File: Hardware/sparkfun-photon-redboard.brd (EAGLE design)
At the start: 68.6 x 53.3 mm, 54 parts, among them J1 AMP FCI 10103594-0001LF, U1 WM-N-BM-14

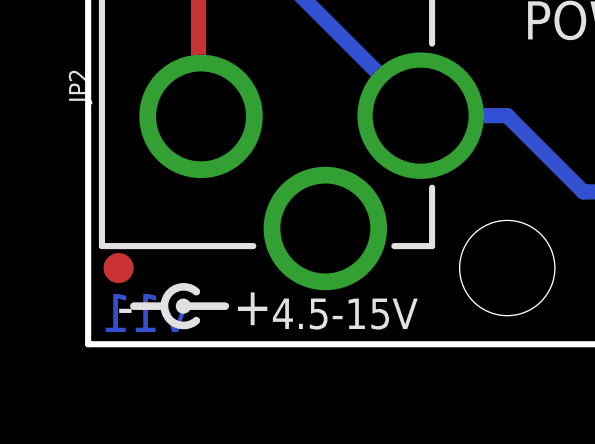
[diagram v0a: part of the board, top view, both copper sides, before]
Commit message: Updated Revision to 2.0 for Reds
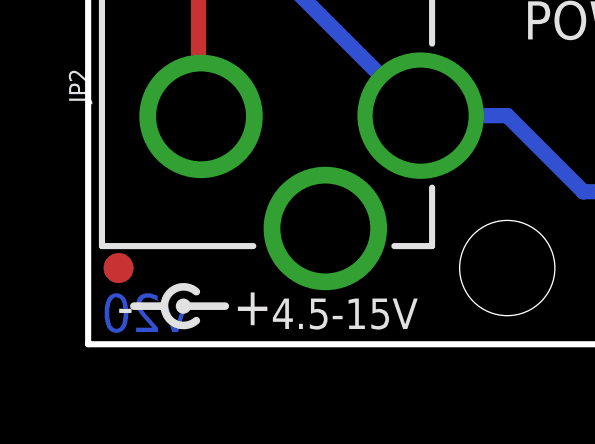
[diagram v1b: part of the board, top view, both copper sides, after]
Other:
- board text added: "v20"
- board text removed: "v11"
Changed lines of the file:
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@@
 <text x="20.32" y="4.064" size="1.27" layer="21" font="vector" ratio="15" rot="R90" align="center-left">VBAT</text>
 <text x="22.86" y="4.064" size="1.27" layer="21" font="vector" ratio="15" rot="R90" align="center-left">GND</text>
-<text x="1.905" y="1.6764" size="1.27" layer="16" font="vector" ratio="15" rot="MR0" align="top-center">v11</text>
+<text x="1.905" y="1.6764" size="1.27" layer="16" font="vector" ratio="15" rot="MR0" align="top-center">v20</text>
 <text x="6.096" y="1.016" size="1.016" layer="21" font="vector" ratio="15" align="center-left">4.5-15V</text>
 <wire x1="1.524" y1="1.27" x2="2.54" y2="1.27" width="0.254" layer="21"/>

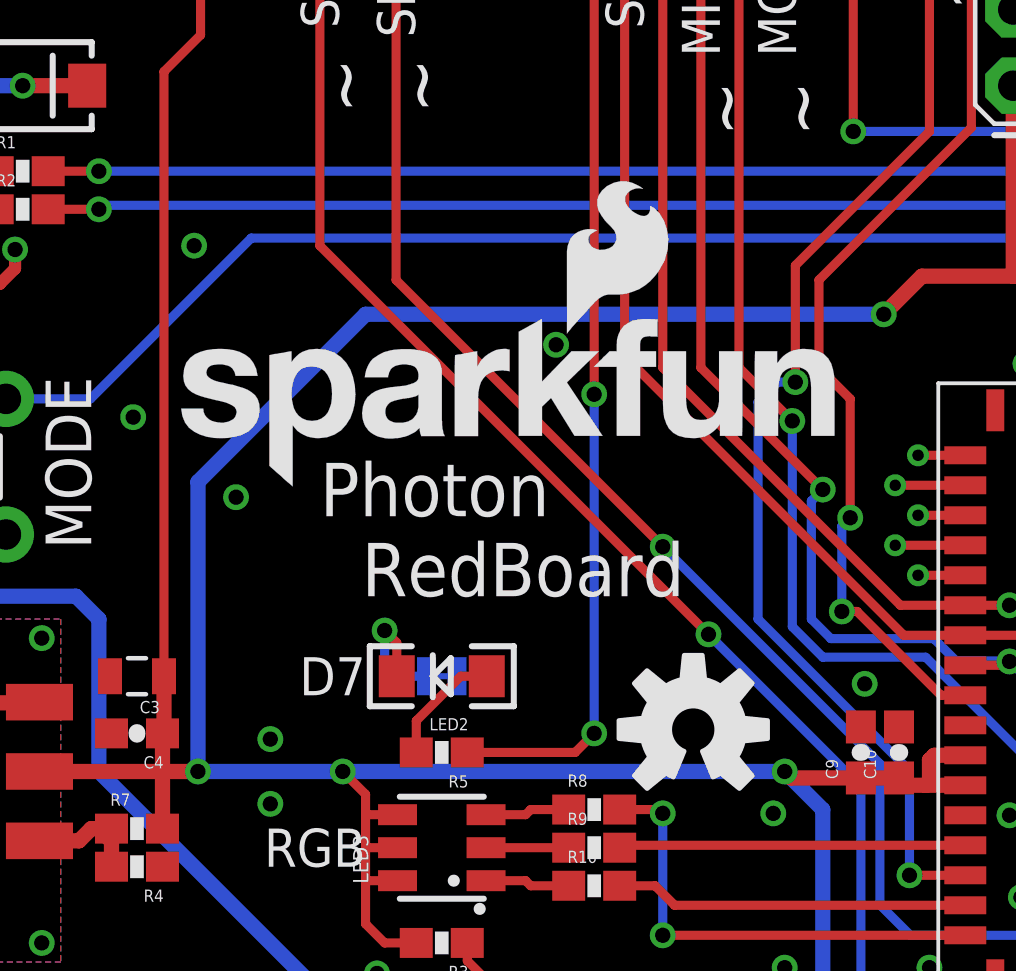
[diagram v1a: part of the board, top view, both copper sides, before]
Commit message: Approved DRC errors
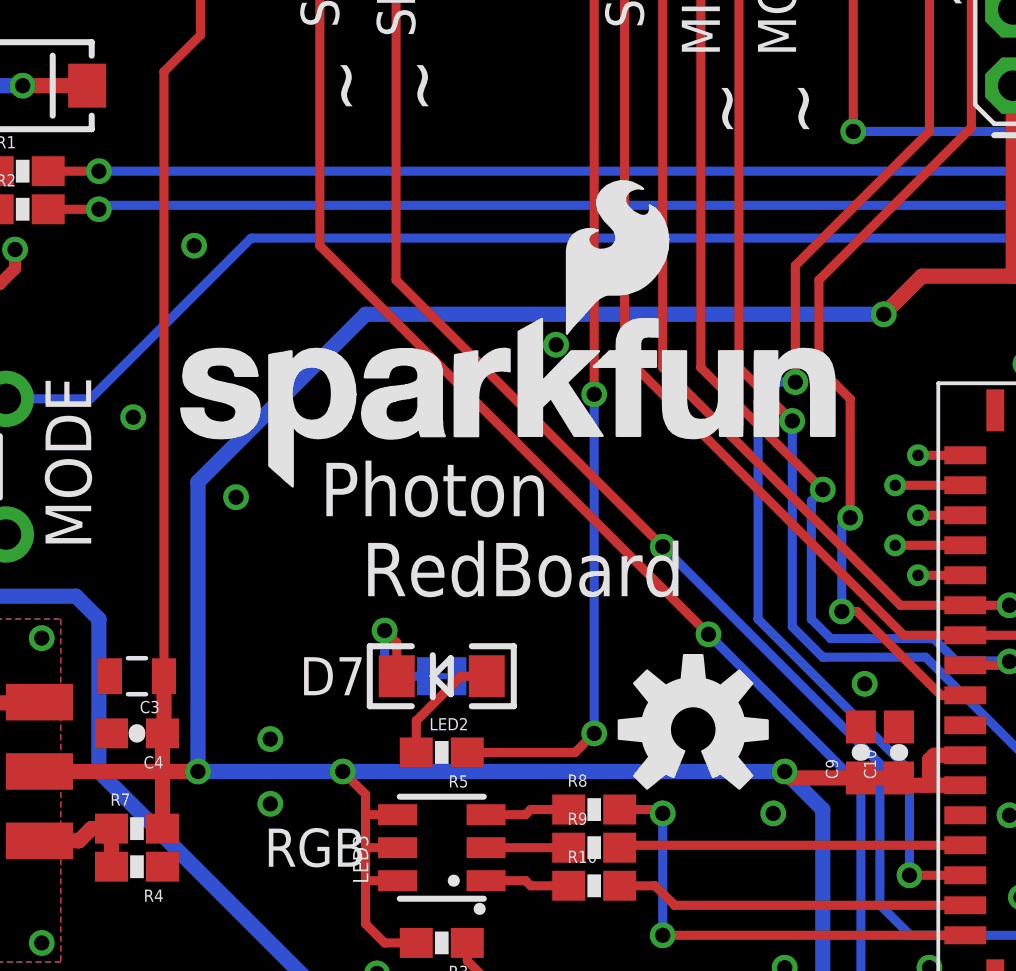
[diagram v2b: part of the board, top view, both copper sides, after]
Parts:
- FRAME1: value (none) -> FRAME-LETTER
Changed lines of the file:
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@@
 <layer number="230" name="230bmp" color="7" fill="1" visible="no" active="yes"/>
 <layer number="231" name="231bmp" color="7" fill="1" visible="no" active="yes"/>
+<layer number="232" name="Eagle3D_PG2" color="7" fill="1" visible="yes" active="yes"/>
+<layer number="233" name="Eagle3D_PG3" color="7" fill="1" visible="yes" active="yes"/>
 <layer number="248" name="Housing" color="7" fill="1" visible="no" active="yes"/>
 <layer number="249" name="Edge" color="7" fill="1" visible="no" active="yes"/>
@@
 </element>
 <element name="JP4" library="SparkFun-Connectors" package="1X02" value="DNP" x="22.86" y="2.54" rot="R180"/>
-<element name="FRAME1" library="SparkFun-Aesthetics" package="CREATIVE_COMMONS" value="" x="15.24" y="-11.43">
-<attribute name="VERSION" value="v01" x="15.24" y="-11.43" size="1.27" layer="27" font="vector" ratio="15" display="off"/>
-<attribute name="DESIGNER" value="Jim Lindblom" x="15.24" y="-11.43" size="1.27" layer="27" font="vector" ratio="15" display="off"/>
-</element>
+<element name="FRAME1" library="SparkFun-Aesthetics" package="CREATIVE_COMMONS" value="FRAME-LETTER" x="15.24" y="-11.43"/>
 <element name="TP3" library="SparkFun-Passives" package="TP_15TH" value="TEST-POINTTP_15TH_THRU" x="53.975" y="22.59" rot="R180"/>
 <element name="TP1" library="SparkFun-Passives" package="TP_15TH" value="TEST-POINTTP_15TH_THRU" x="54.737" y="23.59" rot="R180"/>
